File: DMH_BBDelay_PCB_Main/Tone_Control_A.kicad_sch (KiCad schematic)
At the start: 11 parts, among them U17 TL072

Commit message: Inverted time and tone control pots
... and added AC coupling to the outputs
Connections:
- net at C45.1, R165.2: now also RV11.1; no longer RV11.3
- net at C46.2, R162.1: now also RV11.3; no longer RV11.1
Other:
- moved on the sheet: RV11A
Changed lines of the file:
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@@
 	(symbol
 		(lib_id "Device:R_Potentiometer_Dual_Separate")
-		(at 200.66 55.88 270)
+		(at 200.66 55.88 90)
+		(mirror x)
 		(unit 1)
 		(body_style 1)
@@
 		(in_pos_files yes)
 		(dnp no)
-		(fields_autoplaced yes)
 		(property "Reference" "RV11"
 			(at 200.66 49.53 90)

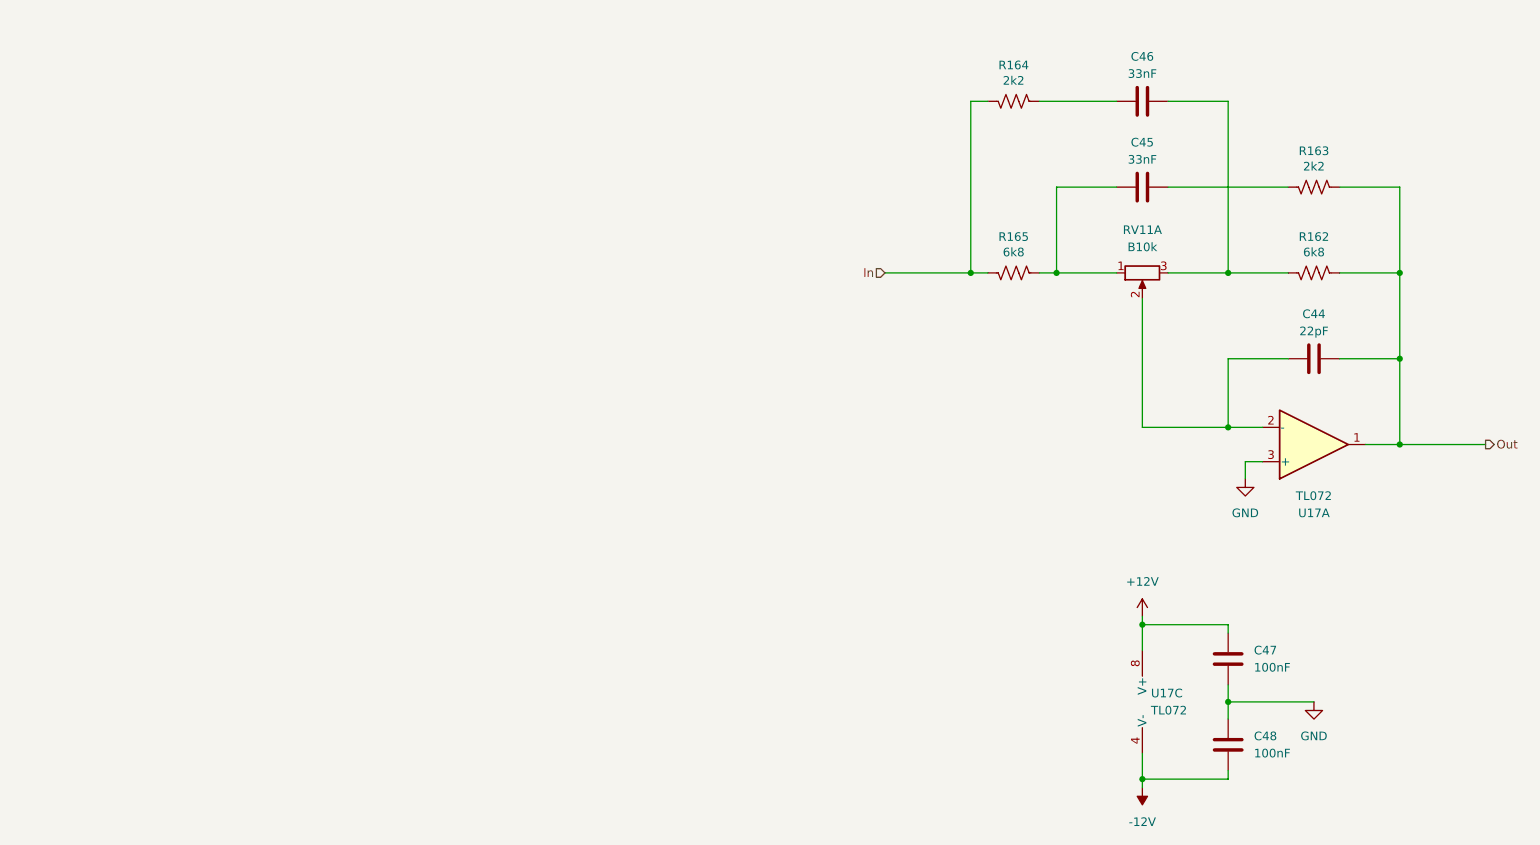
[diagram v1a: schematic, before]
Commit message: Designed input compressor circuits
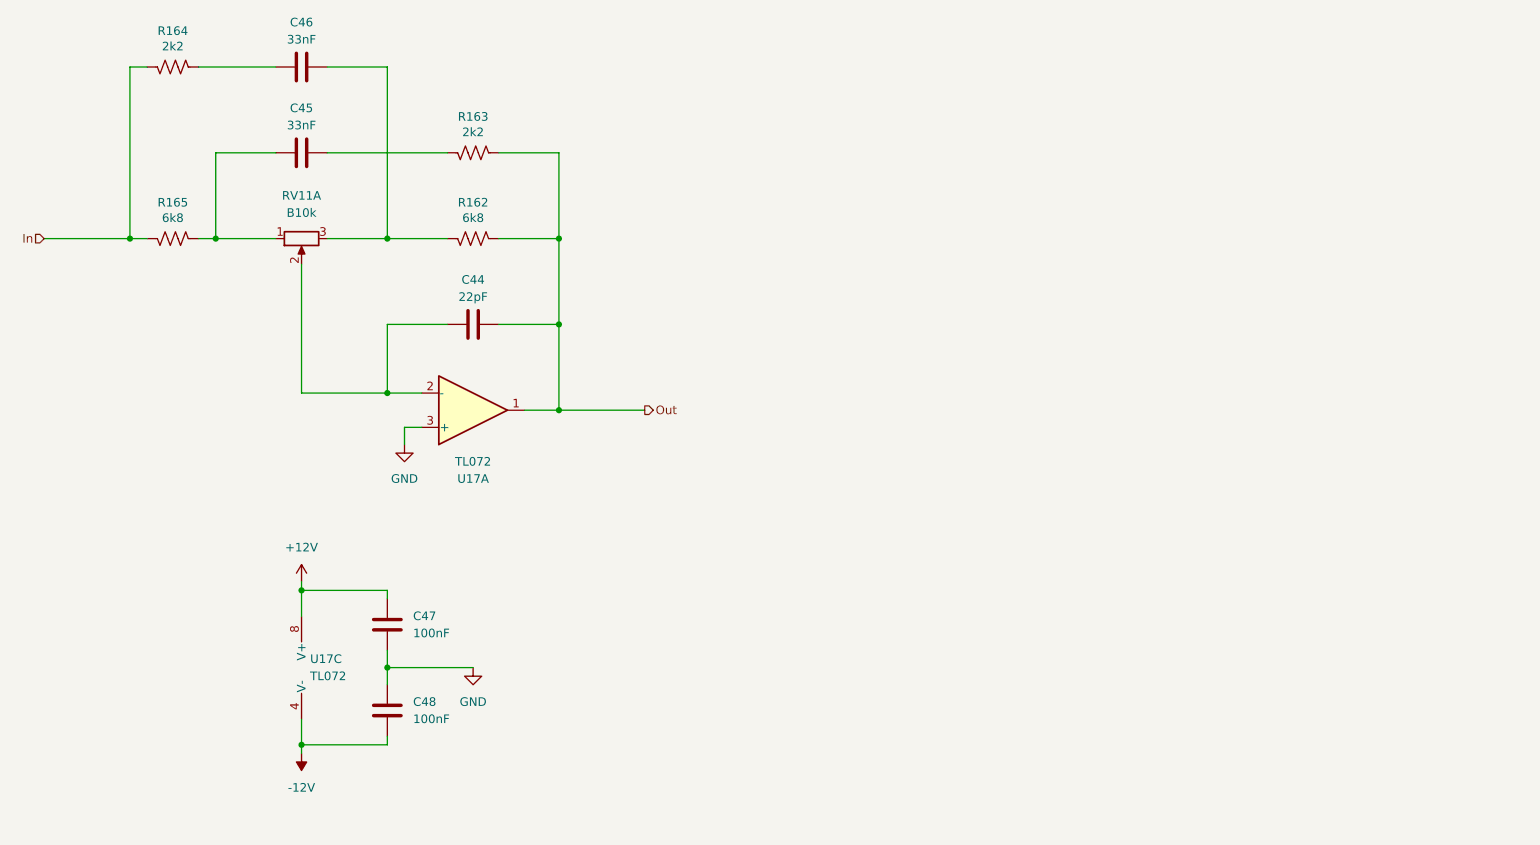
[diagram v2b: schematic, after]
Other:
- moved on the sheet: C44, C45, C46, C47, C48, R162, R163, R164, R165, RV11A, U17A, U17C
